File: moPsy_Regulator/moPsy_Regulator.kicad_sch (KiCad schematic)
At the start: 21 parts, among them J1 Conn_01x01_Pin, J2 Conn_01x01_Pin, J3 Conn_01x01_Pin, J4 Conn_01x01_Pin, Q1 BD201, Q2 BC337, U1 LM723_DIP14

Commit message: First draft of the PCB
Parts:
- D1: value D -> BY 500; footprint (none) -> Diode_THT:D_DO-201_P12.70mm_Horizontal
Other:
- note added: "BY 500-800 DIO"
- note added: "FK-A 2,2M 25B"
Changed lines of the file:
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@@
+		)
+	)
+	(text "BY 500-800 DIO"
+		(exclude_from_sim no)
+		(at 211.328 74.93 0)
+		(effects
+			(font
+				(size 1.27 1.27)
+			)
 		)
 	)
@@
 		)
 	)
+	(text "FK-A 2,2M 25B"
+		(exclude_from_sim no)
+		(at 59.69 33.274 0)
+		(effects
+			(font
+				(size 1.27 1.27)
+			)
+		)
+	)
 	(global_label "V_{in}"
 		(shape output)
@@
 			)
 		)
-		(property "Value" "D"
+		(property "Value" "BY 500"
 			(at 203.2 72.3899 90)
 			(effects
@@
 			)
 		)
-		(property "Footprint" ""
+		(property "Footprint" "Diode_THT:D_DO-201_P12.70mm_Horizontal"
 			(at 200.66 71.12 0)
 			(effects

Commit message: Small fixes and Greographic Renumeration
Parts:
- renumbered C4 to C1, C1 to C4, J4 to J3, J3 to J4
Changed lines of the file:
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@@
 		(dnp no)
 		(fields_autoplaced yes)
-		(property "Reference" "C1"
+		(property "Reference" "C4"
 			(at 256.54 29.5909 0)
 			(effects
@@
 			(project "moPsy_Regulator"
 				(path "/07db4171-bb9d-4d0b-8c69-a93dfdf899ac"
-					(reference "C1")
+					(reference "C4")
 					(unit 1)
 				)
@@
 		(on_board yes)
 		(dnp no)
-		(property "Reference" "C4"
+		(property "Reference" "C1"
 			(at 97.79 105.4099 0)
 			(effects
@@
 			(project "moPsy_Regulator"
 				(path "/07db4171-bb9d-4d0b-8c69-a93dfdf899ac"
-					(reference "C4")
+					(reference "C1")
 					(unit 1)
 				)
@@
 		(dnp no)
 		(fields_autoplaced yes)
-		(property "Reference" "J4"
+		(property "Reference" "J3"
 			(at 273.685 30.48 0)
 			(effects
@@
 			(project "moPsy_Regulator"
 				(path "/07db4171-bb9d-4d0b-8c69-a93dfdf899ac"
-					(reference "J4")
+					(reference "J3")
 					(unit 1)
 				)
@@
 		(dnp no)
 		(fields_autoplaced yes)
-		(property "Reference" "J3"
+		(property "Reference" "J4"
 			(at 273.685 22.86 0)
 			(effects
@@
 			(project "moPsy_Regulator"
 				(path "/07db4171-bb9d-4d0b-8c69-a93dfdf899ac"
-					(reference "J3")
-					(unit 1)
-				)
+					(reference "J4")
+					(unit 1)
+				)

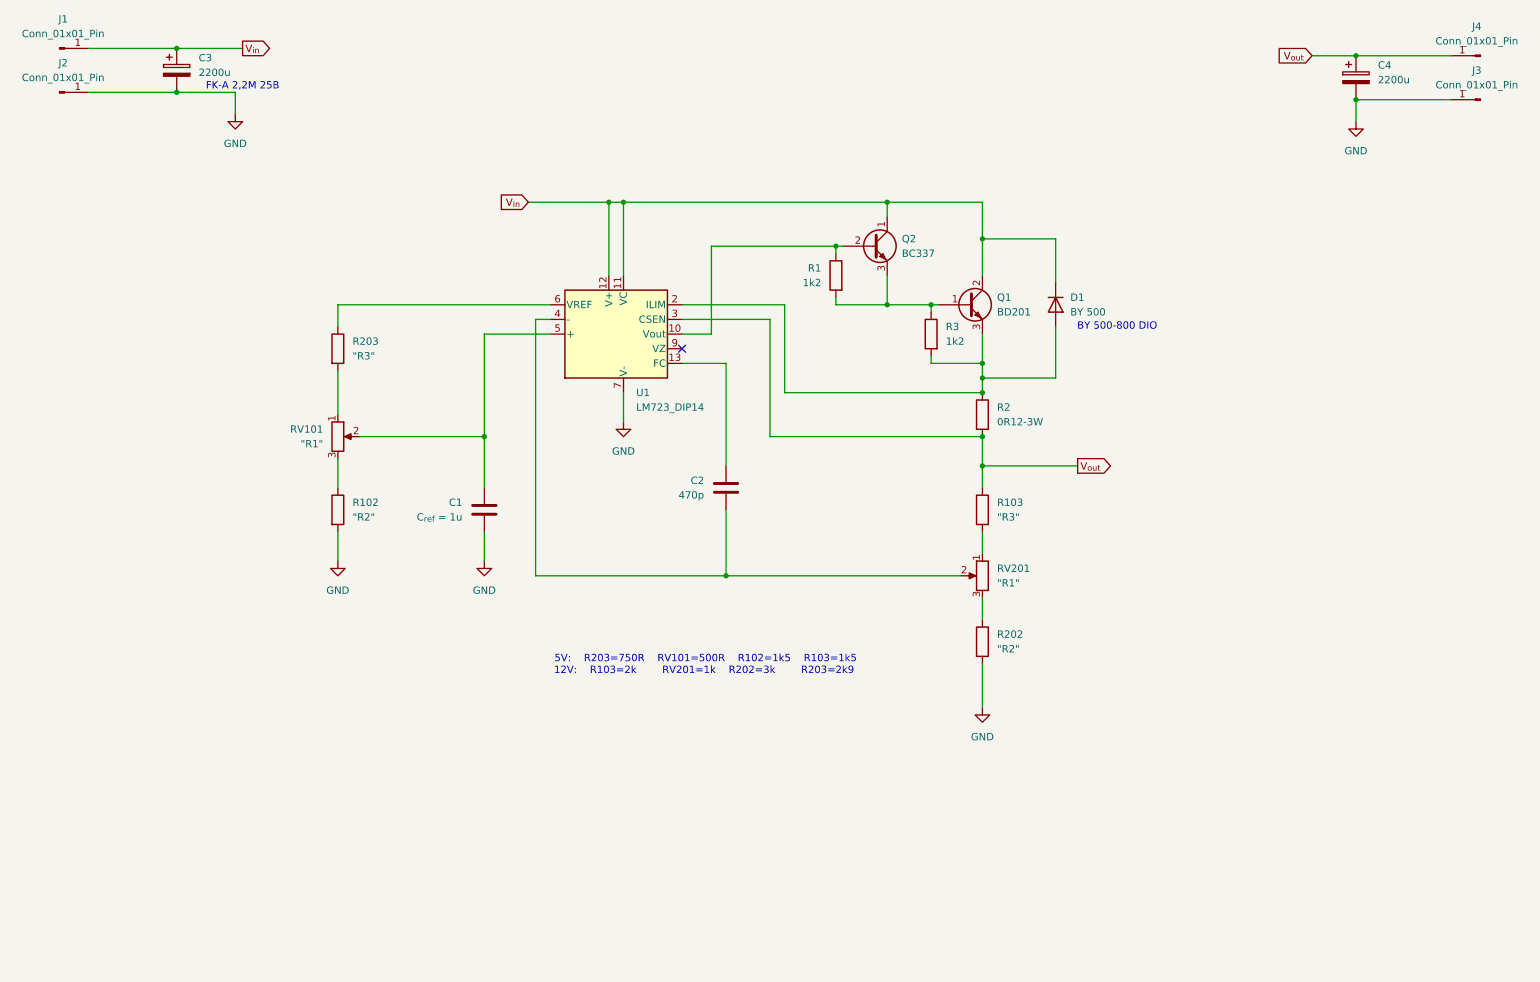
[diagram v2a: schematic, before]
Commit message: Improve the voltage selection and layout
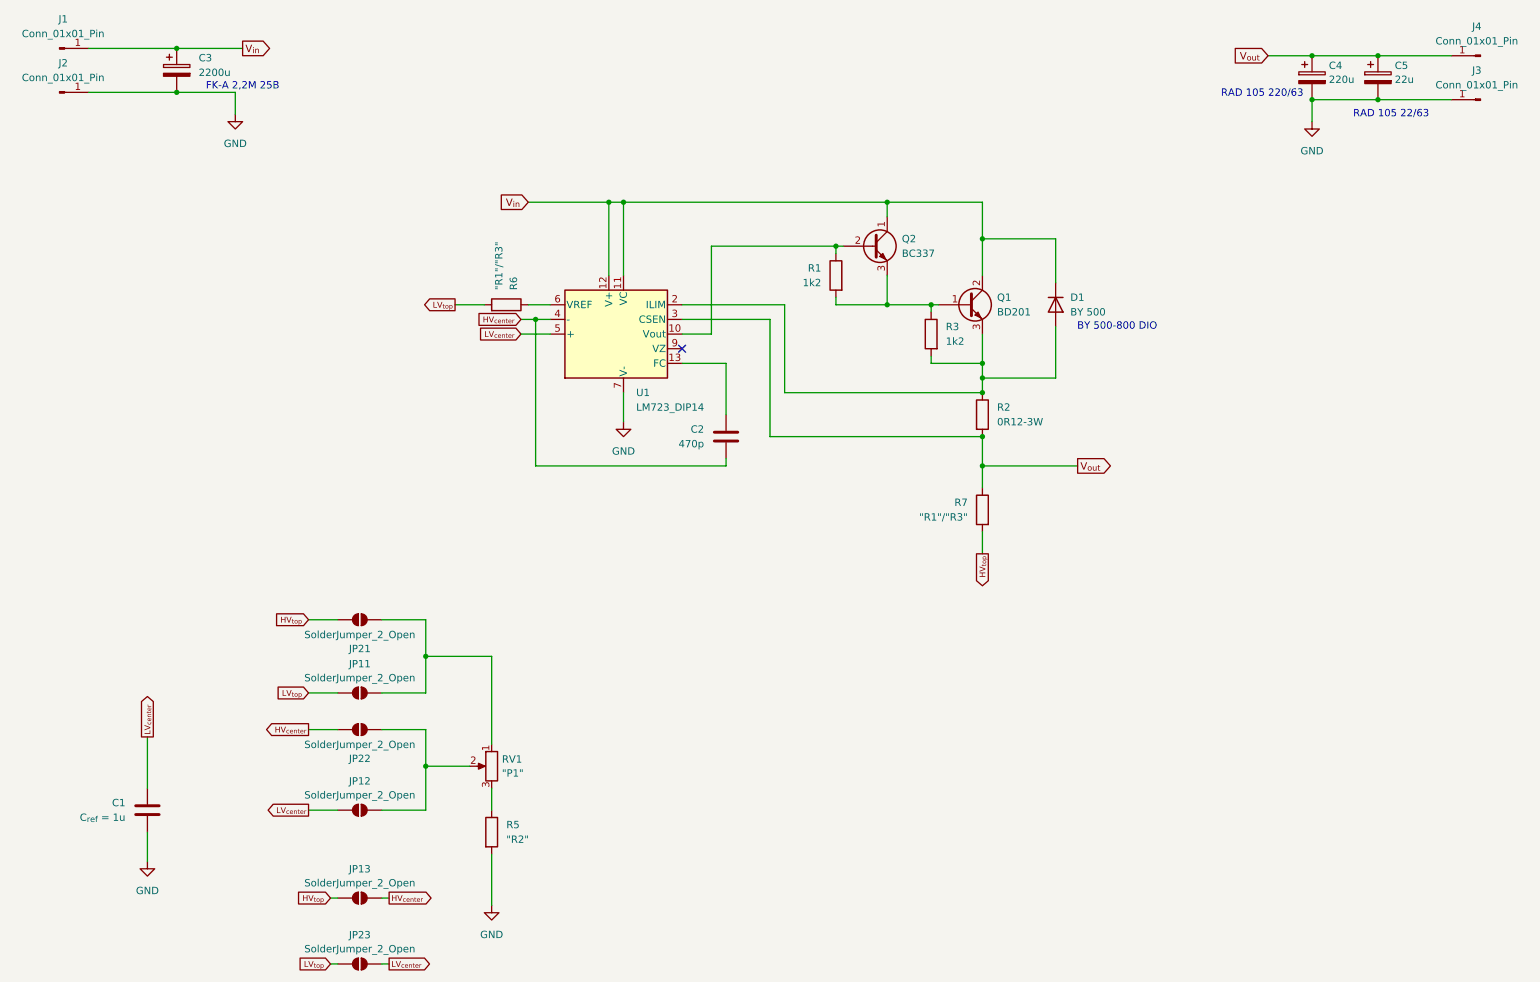
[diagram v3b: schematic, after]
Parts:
- removed R102, R202: "R2", Resistor_THT:R_Axial_DIN0207_L6.3mm_D2.5mm_P7.62mm_Horizontal, symbol Device:R
- removed R103, R203: "R3", Resistor_THT:R_Axial_DIN0207_L6.3mm_D2.5mm_P7.62mm_Horizontal, symbol Device:R
- removed RV101, RV201: "R1", Potentiometer_THT:Potentiometer_Piher_PT-10-V10_Vertical, symbol Device:R_Potentiometer
- added C5: 22u, Capacitor_THT:CP_Radial_D6.3mm_P2.50mm, symbol Device:C_Polarized
- added JP11, JP12, JP13, JP21, JP22, JP23: SolderJumper_2_Open, Jumper:SolderJumper-2_P1.3mm_Open_RoundedPad1.0x1.5mm, symbol Jumper:SolderJumper_2_Open
- added R5: "R2", Resistor_THT:R_Axial_DIN0207_L6.3mm_D2.5mm_P7.62mm_Horizontal, symbol Device:R
- added R6, R7: "R1"/"R3", Resistor_THT:R_Axial_DIN0207_L6.3mm_D2.5mm_P7.62mm_Horizontal, symbol Device:R
- added RV1: "P1", Potentiometer_THT:Potentiometer_Piher_PT-10-V10_Vertical, symbol Device:R_Potentiometer
- C4: value 2200u -> 220u; footprint Capacitor_THT:CP_Radial_D16.0mm_P7.50mm -> Capacitor_THT:CP_Radial_D10.0mm_P5.00mm
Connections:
- net GND: now also C5.2, R5.2
- net V_{out}: now also C5.1, R7.1
- net HV_{center}: now reaches C2.2, U1.4 (-)
- net HV_{center}: now also JP13.2 (B), JP22.1 (A)
- net LV_{center}: now reaches C1.1, U1.5 (+)
- net LV_{center}: now also JP12.1 (A), JP23.2 (B)
- net at U1.6 (VREF): now also R6.1
- new net: JP11.2 (B), JP21.2 (B), RV1.1
- new net: R5.1, RV1.3
- new net: JP12.2 (B), JP22.2 (B), RV1.2
- new net HV_{top}: JP13.1 (A), JP21.1 (A), R7.2
- new net LV_{top}: JP11.1 (A), JP23.1 (A), R6.2
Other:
- note added: "RAD 105 22/63"
- note added: "RAD 105 220/63"
- note removed: "5V: R203=750R RV101=500R R102=1k5 R103=1k5 12V: R103=2k RV201=1k R202=3k R203=2k9"
- moved on the sheet: C1, C2, C4

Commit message: Geographical Reannotation and some minor fixes
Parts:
- renumbered C2 to C1, C1 to C2, C5 to C4, C4 to C5, JP23 to JP1, JP21 to JP2, JP22 to JP3, JP11 to JP4, JP12 to JP5, JP13 to JP6, R7 to R1, R5 to R2, R6 to R3, R1 to R4, R3 to R5, R2 to R6
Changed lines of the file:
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@@
 		(on_board yes)
 		(dnp no)
-		(property "Reference" "JP21"
+		(property "Reference" "JP2"
 			(at 80.01 130.7635 0)
 			(effects
@@
 			(project "moPsy_Regulator"
 				(path "/07db4171-bb9d-4d0b-8c69-a93dfdf899ac"
-					(reference "JP21")
+					(reference "JP2")
 					(unit 1)
 				)
@@
 		(on_board yes)
 		(dnp no)
-		(property "Reference" "R6"
+		(property "Reference" "R3"
 			(at 106.6801 68.58 0)
 			(effects
@@
 			(project "moPsy_Regulator"
 				(path "/07db4171-bb9d-4d0b-8c69-a93dfdf899ac"
-					(reference "R6")
+					(reference "R3")
 					(unit 1)
 				)
@@
 		(dnp no)
 		(fields_autoplaced yes)
-		(property "Reference" "JP23"
+		(property "Reference" "JP1"
 			(at 80.01 180.3865 0)
 			(effects
@@
 			(project "moPsy_Regulator"
 				(path "/07db4171-bb9d-4d0b-8c69-a93dfdf899ac"
-					(reference "JP23")
+					(reference "JP1")
 					(unit 1)
 				)
@@
 		(dnp no)
 		(fields_autoplaced yes)
-		(property "Reference" "R5"
+		(property "Reference" "R2"
 			(at 105.41 161.2899 0)
 			(effects
@@
 			(project "moPsy_Regulator"
 				(path "/07db4171-bb9d-4d0b-8c69-a93dfdf899ac"
-					(reference "R5")
+					(reference "R2")
 					(unit 1)
 				)
@@
 		(on_board yes)
 		(dnp no)
-		(property "Reference" "R7"
+		(property "Reference" "R1"
 			(at 185.42 105.4099 0)
 			(effects
@@
 			(project "moPsy_Regulator"
 				(path "/07db4171-bb9d-4d0b-8c69-a93dfdf899ac"
-					(reference "R7")
+					(reference "R1")
 					(unit 1)
 				)
@@
 		(dnp no)
 		(fields_autoplaced yes)
-		(property "Reference" "C4"
+		(property "Reference" "C5"
 			(at 248.031 29.6488 0)
 			(effects
@@
 			(project "moPsy_Regulator"
 				(path "/07db4171-bb9d-4d0b-8c69-a93dfdf899ac"
-					(reference "C4")
+					(reference "C5")
 					(unit 1)
 				)
@@
 		(on_board yes)
 		(dnp no)
-		(property "Reference" "C1"
+		(property "Reference" "C2"
 			(at 39.37 157.4799 0)
 			(effects
@@
 			(project "moPsy_Regulator"
 				(path "/07db4171-bb9d-4d0b-8c69-a93dfdf899ac"
-					(reference "C1")
+					(reference "C2")
 					(unit 1)
 				)
@@
 		(dnp no)
 		(fields_autoplaced yes)
-		(property "Reference" "R2"
+		(property "Reference" "R6"
 			(at 190.5 88.8999 0)
 			(effects
@@
 			(project "moPsy_Regulator"
 				(path "/07db4171-bb9d-4d0b-8c69-a93dfdf899ac"
-					(reference "R2")
+					(reference "R6")
 					(unit 1)
 				)
@@
 		(dnp no)
 		(fields_autoplaced yes)
-		(property "Reference" "JP13"
+		(property "Reference" "JP6"
 			(at 80.01 168.9565 0)
 			(effects
@@
 			(project "moPsy_Regulator"
 				(path "/07db4171-bb9d-4d0b-8c69-a93dfdf899ac"
-					(reference "JP13")
+					(reference "JP6")
 					(unit 1)
 				)
@@
 		(on_board yes)
 		(dnp no)
-		(property "Reference" "JP22"
+		(property "Reference" "JP3"
 			(at 80.01 149.8135 0)
 			(effects
@@
 			(project "moPsy_Regulator"
 				(path "/07db4171-bb9d-4d0b-8c69-a93dfdf899ac"
-					(reference "JP22")
+					(reference "JP3")
 					(unit 1)
 				)
@@
 		(on_board yes)
 		(dnp no)
-		(property "Reference" "R1"
+		(property "Reference" "R4"
 			(at 160.02 64.7699 0)
 			(effects
@@
 			(project "moPsy_Regulator"
 				(path "/07db4171-bb9d-4d0b-8c69-a93dfdf899ac"
-					(reference "R1")
+					(reference "R4")
 					(unit 1)
 				)
@@
 		(dnp no)
 		(fields_autoplaced yes)
-		(property "Reference" "JP11"
+		(property "Reference" "JP4"
 			(at 80.01 133.3965 0)
 			(effects
@@
 			(project "moPsy_Regulator"
 				(path "/07db4171-bb9d-4d0b-8c69-a93dfdf899ac"
-					(reference "JP11")
+					(reference "JP4")
 					(unit 1)
 				)
@@
 		(dnp no)
 		(fields_autoplaced yes)
-		(property "Reference" "C5"
+		(property "Reference" "C4"
 			(at 259.461 29.6488 0)
 			(effects
@@
 			(project "moPsy_Regulator"
 				(path "/07db4171-bb9d-4d0b-8c69-a93dfdf899ac"
-					(reference "C5")
+					(reference "C4")
 					(unit 1)
 				)
@@
 		(on_board yes)
 		(dnp no)
-		(property "Reference" "JP12"
+		(property "Reference" "JP5"
 			(at 80.01 153.7165 0)
 			(effects
@@
 			(project "moPsy_Regulator"
 				(path "/07db4171-bb9d-4d0b-8c69-a93dfdf899ac"
-					(reference "JP12")
+					(reference "JP5")
 					(unit 1)
 				)
@@
 		(on_board yes)
 		(dnp no)
-		(property "Reference" "C2"
+		(property "Reference" "C1"
 			(at 139.7 92.7099 0)
 			(effects
@@
 			(project "moPsy_Regulator"
 				(path "/07db4171-bb9d-4d0b-8c69-a93dfdf899ac"
-					(reference "C2")
+					(reference "C1")
 					(unit 1)
 				)
@@
 		(dnp no)
 		(fields_autoplaced yes)
-		(property "Reference" "R3"
+		(property "Reference" "R5"
 			(at 181.61 74.9299 0)
 			(effects
@@
 			(project "moPsy_Regulator"
 				(path "/07db4171-bb9d-4d0b-8c69-a93dfdf899ac"
-					(reference "R3")
-					(unit 1)
-				)
+					(reference "R5")
+					(unit 1)
+				)

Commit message: Improve the circuit
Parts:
- removed JP1, JP2, JP3, JP4, JP5, JP6: SolderJumper_2_Open, Jumper:SolderJumper-2_P1.3mm_Open_RoundedPad1.0x1.5mm, symbol Jumper:SolderJumper_2_Open
- removed R1, R3: "R1"/"R3", Resistor_THT:R_Axial_DIN0207_L6.3mm_D2.5mm_P7.62mm_Horizontal, symbol Device:R
- added D2: 1N4001, Diode_THT:D_DO-41_SOD81_P7.62mm_Horizontal, symbol Device:D
- added R7, R8: 2k7 1%, Resistor_THT:R_Axial_DIN0207_L6.3mm_D2.5mm_P7.62mm_Horizontal, symbol Device:R
- R2: value "R2" -> 1k
- RV1: value "P1" -> 5k
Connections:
- net HV_{center} is gone; now on an unnamed net: C1.2, U1.4 (-)
- net GND: now also R8.2
- net V_{in}: now also D2.2 (A); no longer U1.11 (VC), U1.12 (V+)
- net V_{out}: now also RV1.1; no longer C5.1
- net at U1.6 (VREF): now also R7.1
- net LV_{center}: no longer names the net of C2.1, U1.5 (+)
- net LV_{center}: now also R7.2, R8.1
- new net: C5.1, D2.1 (K), U1.11 (VC), U1.12 (V+)
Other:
- moved on the sheet: C2, C5, D1, Q1, Q2, R2, R4, R5, R6, RV1
